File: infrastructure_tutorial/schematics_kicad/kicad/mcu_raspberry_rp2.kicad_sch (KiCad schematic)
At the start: 0 parts

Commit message: Cleanup images
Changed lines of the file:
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@@
 		(comment 1 "The MIT License (MIT)")
 	)
-	(hierarchical_label "26 {slash} GP20 {slash} trigger1"
+	(hierarchical_label "GP20 {slash} trigger1"
 		(shape input)
 		(at 82.55 64.77 0)
@@
 		)
 	)
-	(hierarchical_label "25 {slash} GP19 {slash} SCL"
+	(hierarchical_label "GP19 {slash} SCL"
 		(shape input)
-		(at 82.55 86.36 0)
+		(at 82.55 83.82 0)
 		(fields_autoplaced yes)
 		(effects
@@
 		)
 	)
-	(hierarchical_label "19 {slash} GP14 {slash} onewire"
+	(hierarchical_label "GP14 {slash} onewire"
 		(shape input)
-		(at 82.55 91.44 0)
+		(at 82.55 87.63 0)
 		(fields_autoplaced yes)
 		(effects
@@
 		)
 	)
-	(hierarchical_label "24 {slash} GP18 {slash} SDA"
+	(hierarchical_label "GP18 {slash} SDA"
 		(shape input)
-		(at 82.55 81.28 0)
+		(at 82.55 80.01 0)
 		(fields_autoplaced yes)
 		(effects
@@
 		)
 	)
-	(hierarchical_label "22 {slash} GP17 {slash} RX"
+	(hierarchical_label "GP17 {slash} RX"
 		(shape input)
 		(at 82.55 76.2 0)
@@
 		)
 	)
-	(hierarchical_label "27 {slash} GP21 {slash} trigger2"
+	(hierarchical_label "GP21 {slash} trigger2"
 		(shape input)
 		(at 82.55 68.58 0)
@@
 		)
 	)
-	(hierarchical_label "21 {slash} GP16 {slash} TX"
+	(hierarchical_label "GP16 {slash} TX"
 		(shape input)
 		(at 82.55 72.39 0)

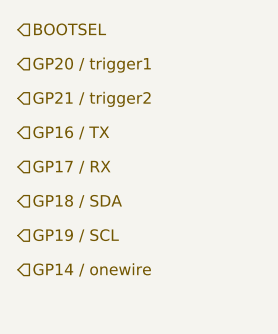
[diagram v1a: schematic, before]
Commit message: Connect pyboard/pico to ground
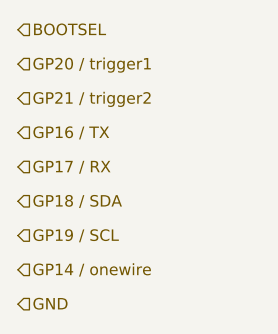
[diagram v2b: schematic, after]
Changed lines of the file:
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@@
 		(comment 1 "The MIT License (MIT)")
+	)
+	(hierarchical_label "GND"
+		(shape input)
+		(at 82.55 91.44 0)
+		(fields_autoplaced yes)
+		(effects
+			(font
+				(size 1.27 1.27)
+			)
+			(justify left)
+		)
 	)
 	(hierarchical_label "GP20 {slash} trigger1"
